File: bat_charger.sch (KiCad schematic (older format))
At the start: 56 parts, among them J1 Vcc In, Q1 Q_PMOS_GDS, Q2 Q_PMOS_GDS, Q3 FDD86580-F085, Q4 FDD86580-F085, SW1 Reset, SW2 Select CE, U1 BQ24618RGET

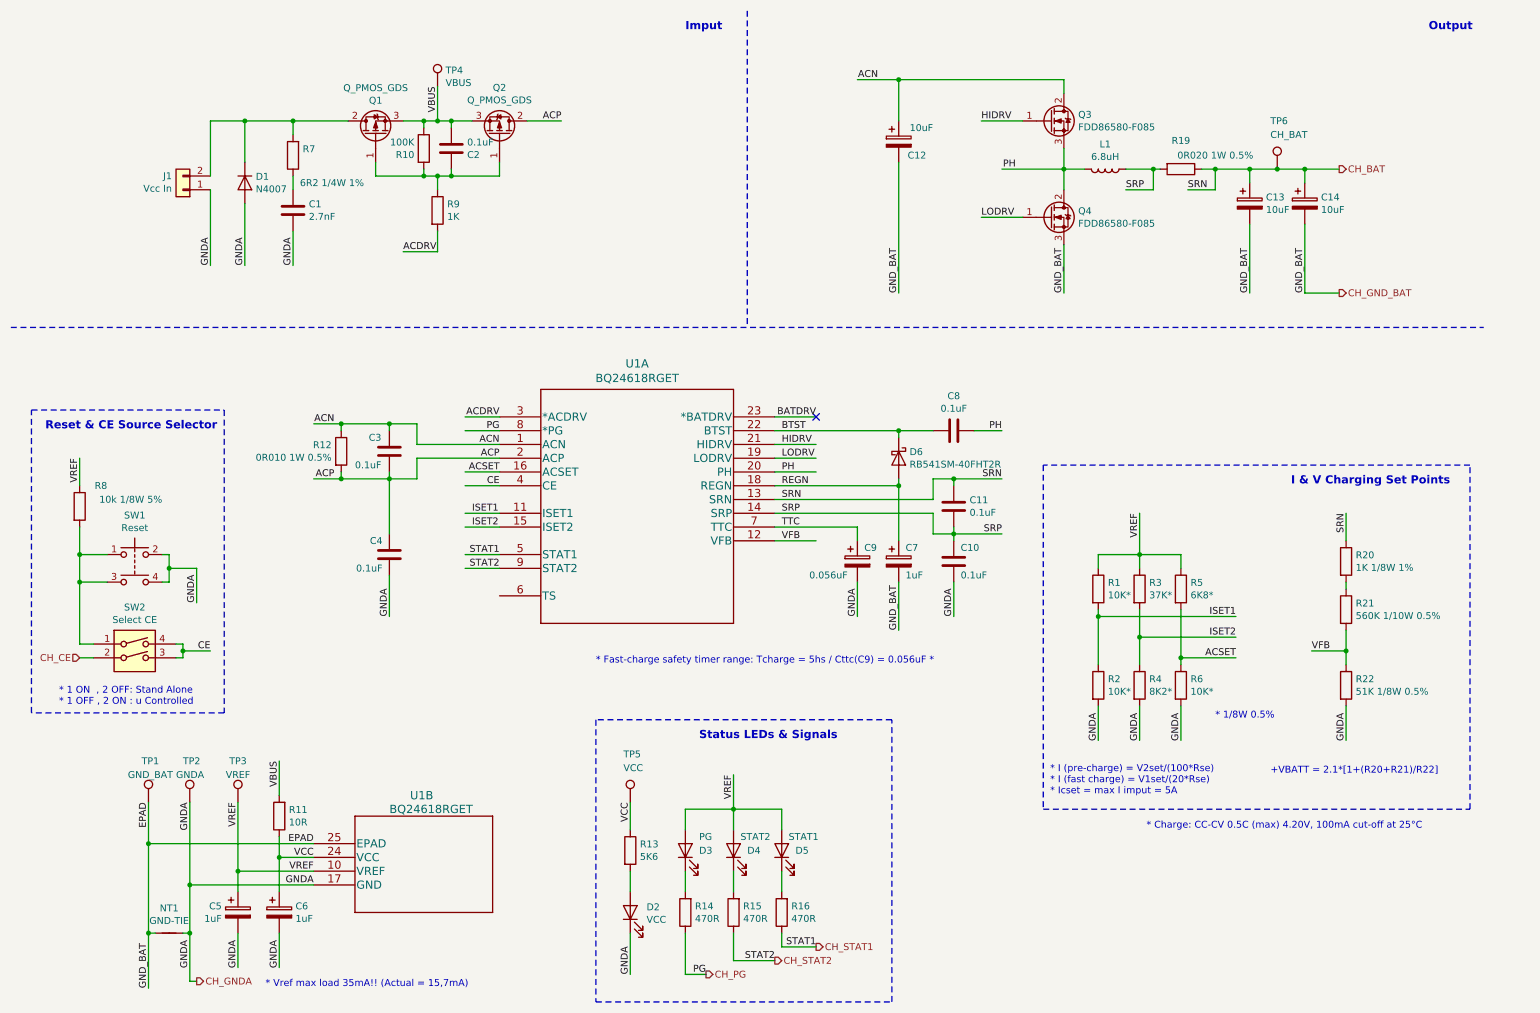
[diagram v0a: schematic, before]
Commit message: Added bat_charger.sch to main hierarchical bms project
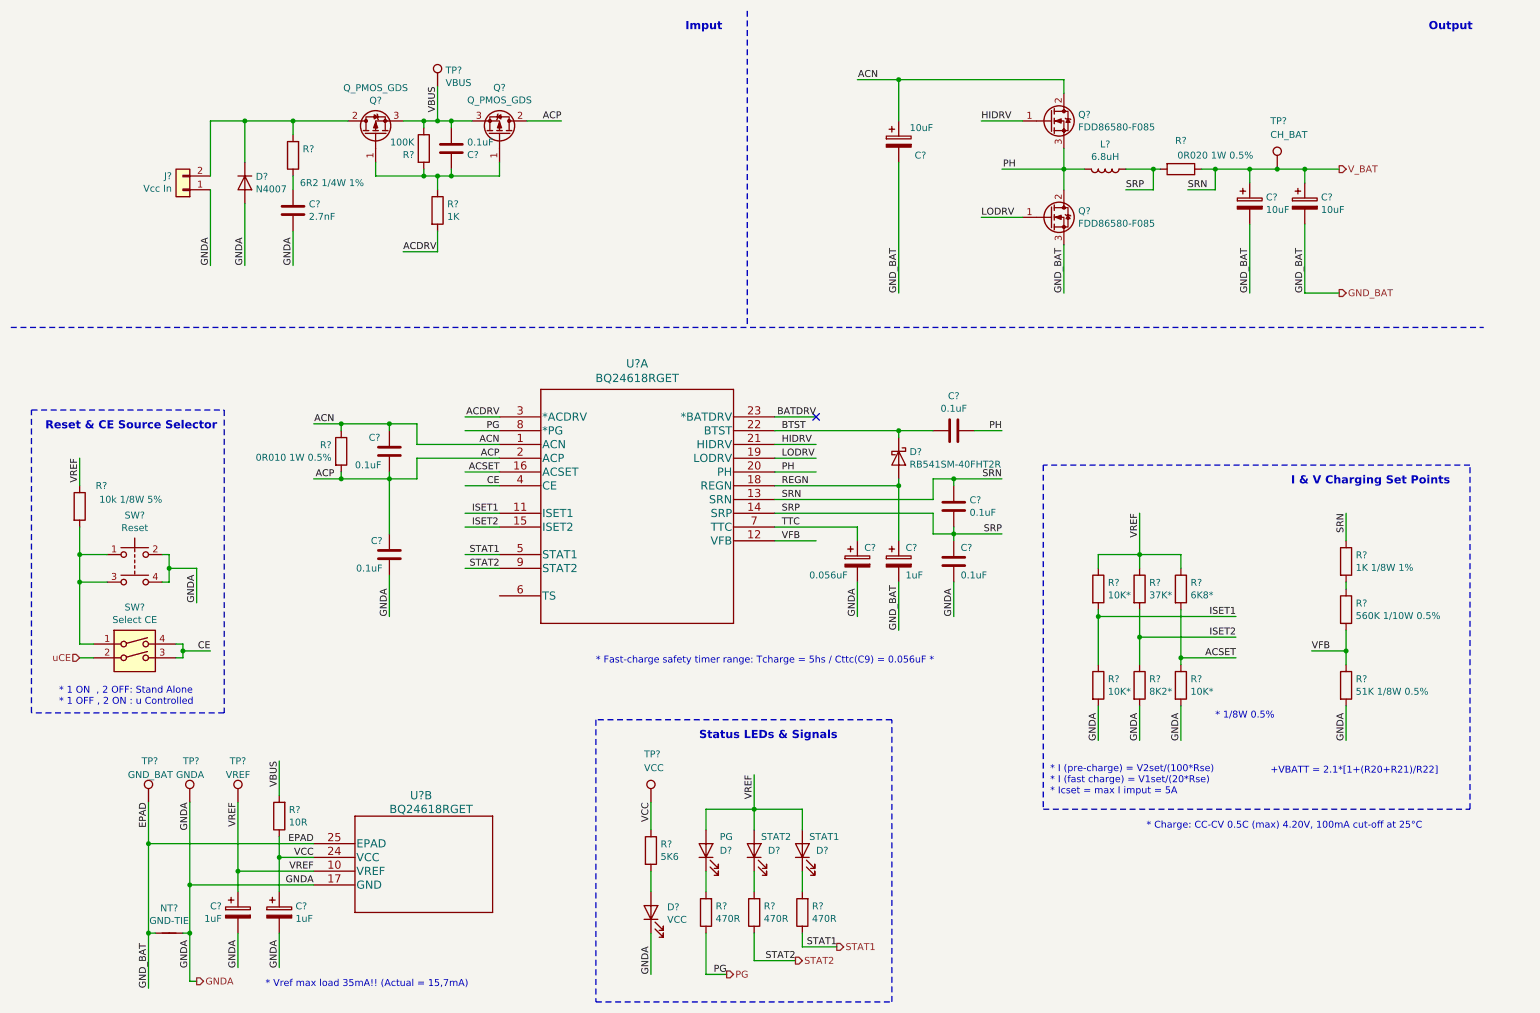
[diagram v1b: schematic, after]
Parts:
- renumbered C1 to C?, C2 to C?, C3 to C?, C4 to C?, C5 to C?, C9 to C?, C7 to C?, C8 to C?, C11 to C?, C10 to C?, C13 to C?, C14 to C?, C6 to C?, C12 to C?, D1 to D?, D2 to D?, D6 to D?, D5 to D?, D4 to D?, D3 to D?, J1 to J?, L1 to L?, NT1 to NT?, Q1 to Q?, Q2 to Q?, Q3 to Q?, Q4 to Q?, R7 to R?, R13 to R?, R10 to R?, R12 to R?, R11 to R?, R16 to R?, R15 to R?, R22 to R?, R21 to R?, R14 to R?, R20 to R?, R1 to R?, R2 to R?, R3 to R?, R4 to R?, R5 to R?, R6 to R?, R9 to R?, R8 to R?, R19 to R?, SW1 to SW?, SW2 to SW?, TP3 to TP?, TP4 to TP?, TP5 to TP?, TP6 to TP?, TP2 to TP?, TP1 to TP?, U1 to U?
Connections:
- net labels added: V_BAT, uCE
- net labels removed: CH_BAT, CH_CE, CH_GNDA, CH_GND_BAT, CH_PG, CH_STAT1, CH_STAT2
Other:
- moved on the sheet: D?, R?, TP?

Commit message: Charger Temperature Sensor bypassed!
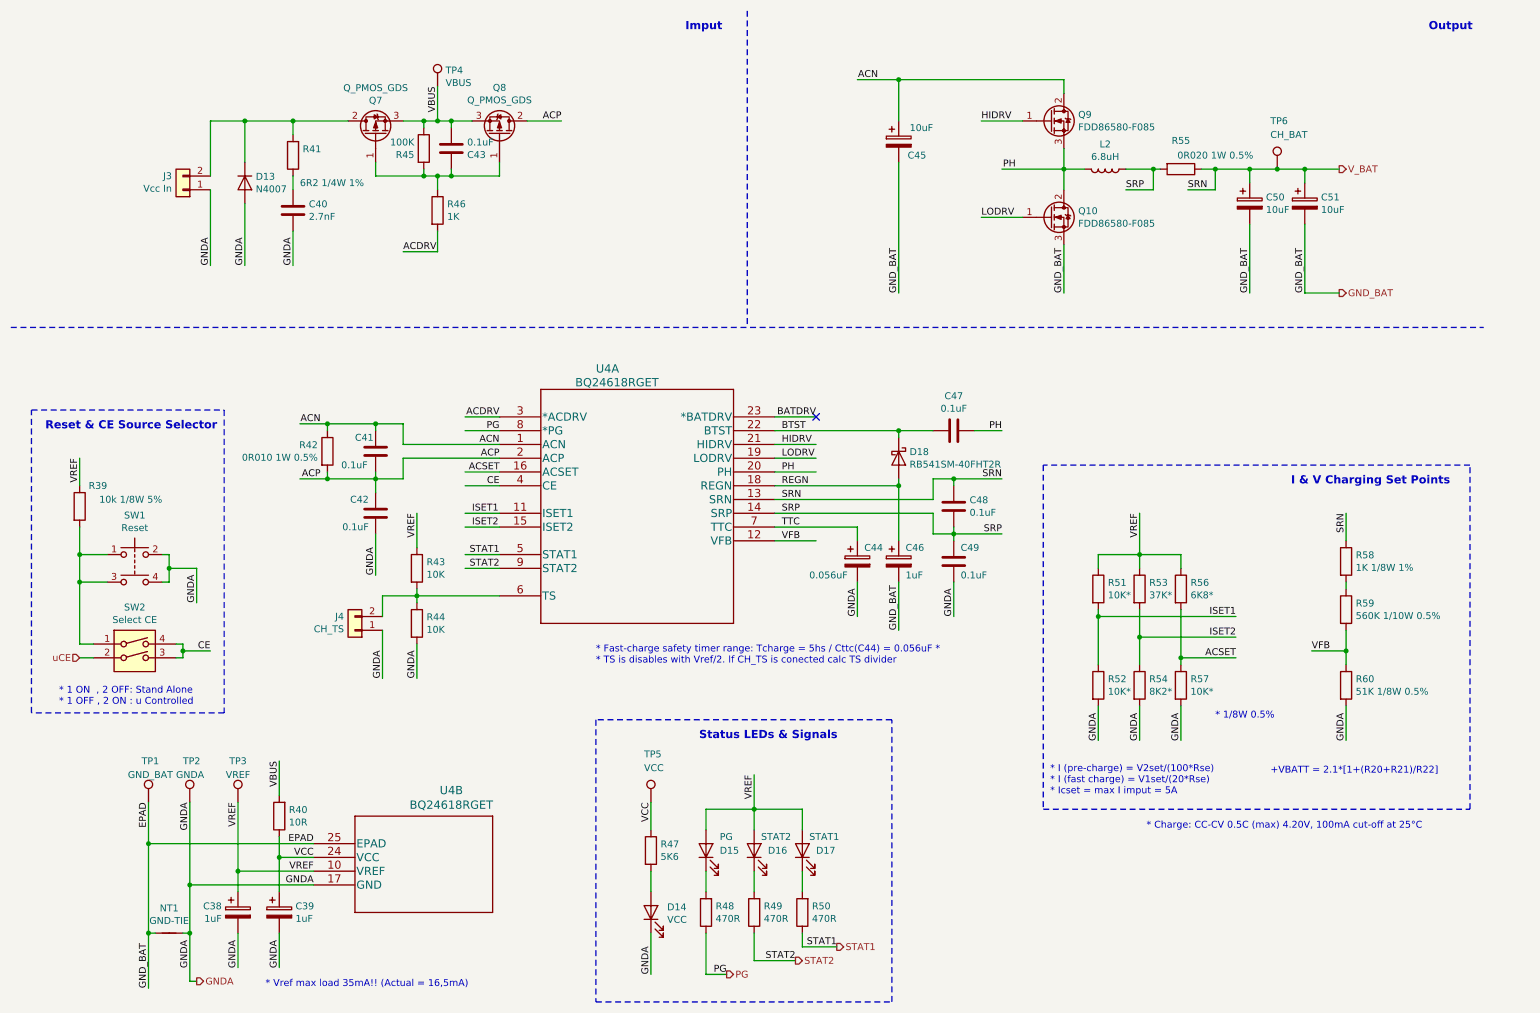
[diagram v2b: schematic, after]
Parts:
- added J4: CH_TS, Connector_JST:JST_XH_S7B-XH-A_1x07_P2.50mm_Horizontal, symbol Connector_Generic:Conn_01x02
- added R43, R44: 10K, Resistors_SMD:R_0805_HandSoldering, symbol Device:R
- gave numbers to parts that had none: 56
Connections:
- wire segments 190 -> 198
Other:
- note added: "* Fast-charge safety timer range: Tcharge = 5hs / Cttc(C44) = 0.056uF *\n* TS is disables with Vref/2. If CH_TS is conected calc TS divider"
- note added: "* Vref max load 35mA!! (Actual = 16,5mA)\n"
- note removed: "* Fast-charge safety timer range: Tcharge = 5hs / Cttc(C9) = 0.056uF *"
- note removed: "* Vref max load 35mA!! (Actual = 15,7mA)\n"
- moved on the sheet: C41, C42, R42

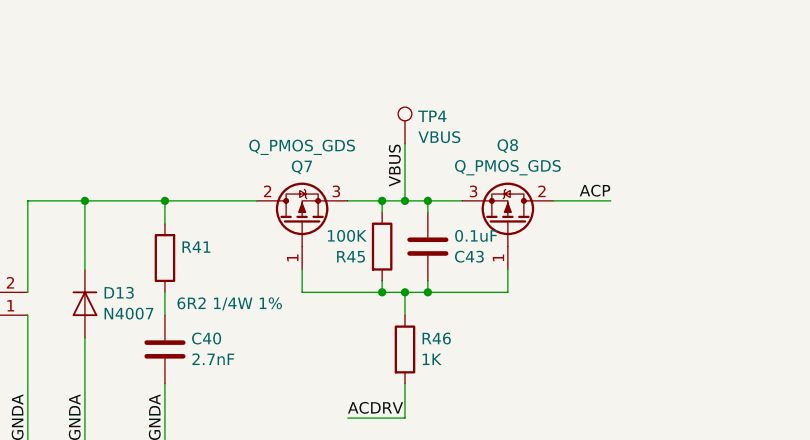
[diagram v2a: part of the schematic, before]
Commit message: Reserved mcu CAN pins & edited MOS names on Bat_charger
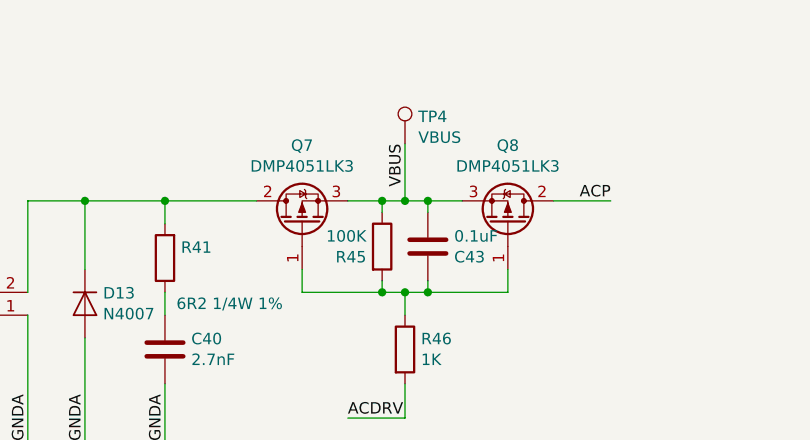
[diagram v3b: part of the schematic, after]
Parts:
- Q7, Q8: value Q_PMOS_GDS -> DMP4051LK3
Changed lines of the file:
@@
 P 4050 1400
 F 0 "Q8" V 4392 1400 50  0000 C CNN
-F 1 "Q_PMOS_GDS" V 4301 1400 50  0000 C CNN
+F 1 "DMP4051LK3" V 4301 1400 50  0000 C CNN
 F 2 "TO_SOT_Packages_SMD:TO-252-2_Rectifier" H 4250 1500 50  0001 C CNN
 F 3 "https://ar.mouser.com/ProductDetail/DMP4051LK3-13" H 4050 1400 50  0001 C CNN
@@
 U 1 1 5FC778CF
 P 3150 1400
-F 0 "Q7" V 3399 1400 50  0000 C CNN
-F 1 "Q_PMOS_GDS" V 3490 1400 50  0000 C CNN
+F 0 "Q7" V 3492 1400 50  0000 C CNN
+F 1 "DMP4051LK3" V 3401 1400 50  0000 C CNN
 F 2 "TO_SOT_Packages_SMD:TO-252-2_Rectifier" H 3350 1500 50  0001 C CNN
 F 3 "https://ar.mouser.com/ProductDetail/DMP4051LK3-13" H 3150 1400 50  0001 C CNN
